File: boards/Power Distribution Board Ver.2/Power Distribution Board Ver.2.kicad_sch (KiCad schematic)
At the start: 89 parts, among them J1 Screw_Terminal_01x02, J2 Screw_Terminal_01x06, J3 Screw_Terminal_01x06, J4 Screw_Terminal_01x06, K1 Relay, K2 Relay, K3 Relay, K4 Relay, K5 Relay, K6 Relay, SW1 SW_Push_Open, U1 SIC431AED-T1-GE3, U2 SIC431AED-T1-GE3, U3 SIC431AED-T1-GE3

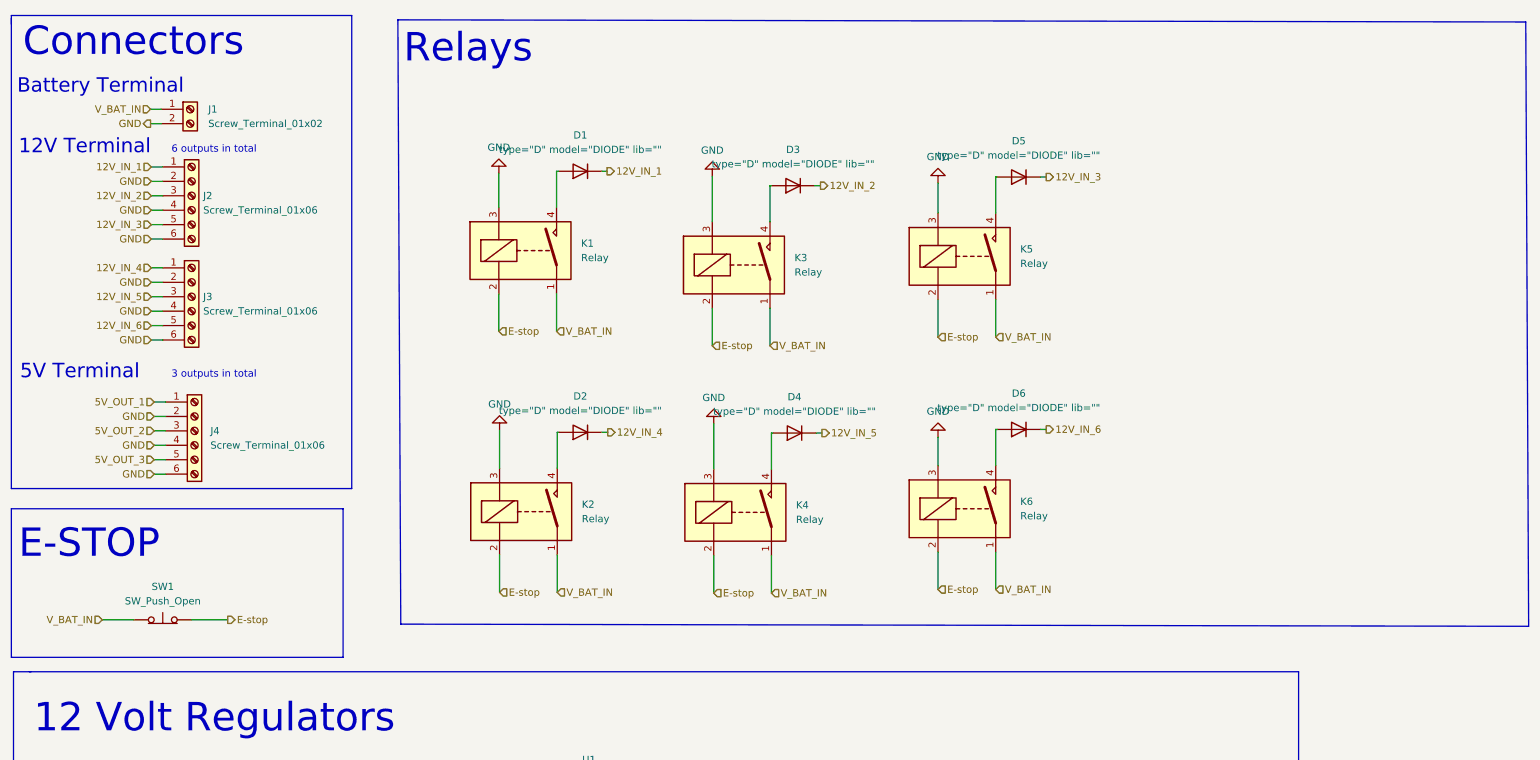
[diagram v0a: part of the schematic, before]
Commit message: 12v relay footprint and updated board wiring
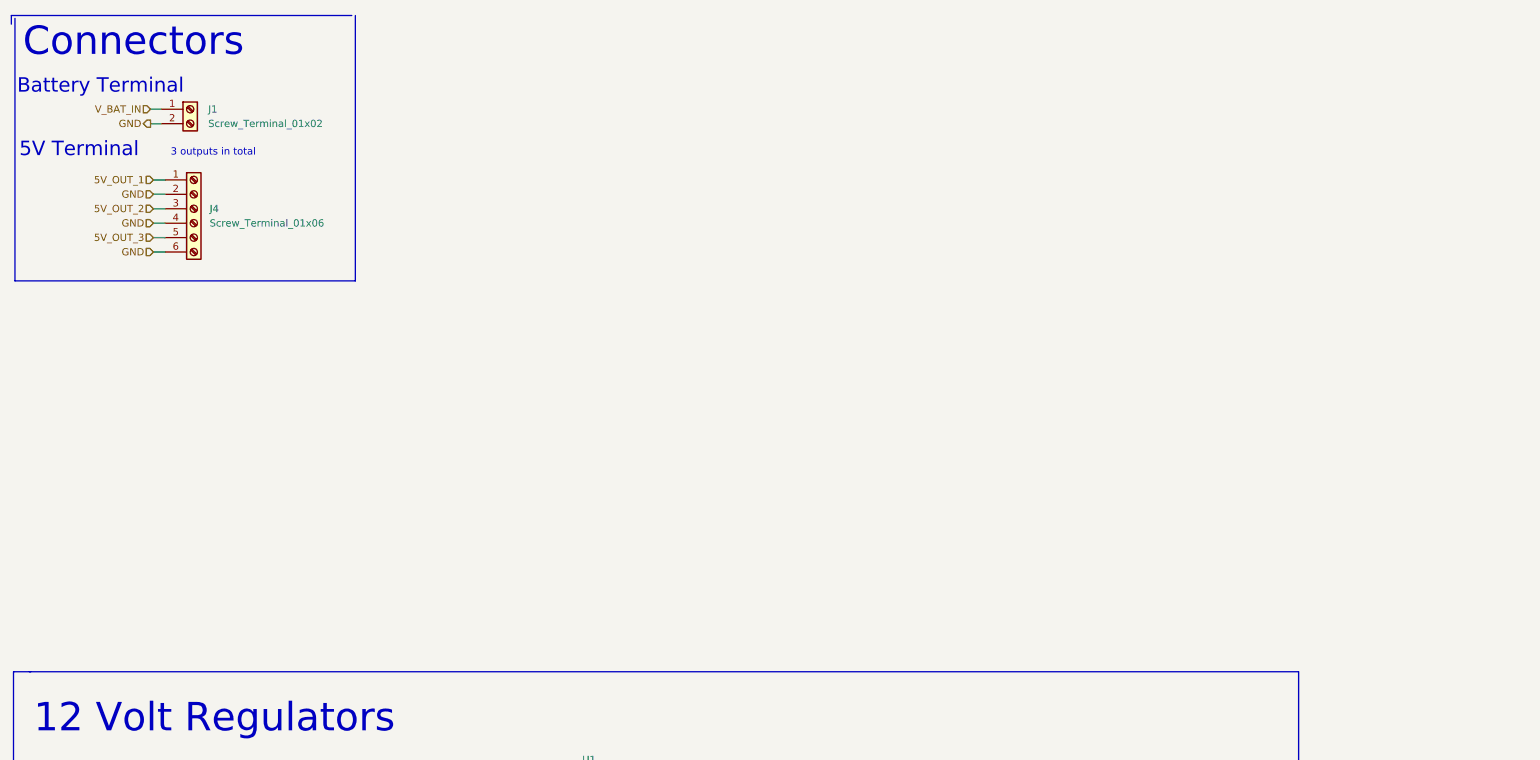
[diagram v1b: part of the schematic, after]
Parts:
- removed D1, D2, D3, D4, D5, D6: ${SIM.PARAMS}, Package_TO_SOT_SMD:TO-263-2, symbol Simulation_SPICE:DIODE
- removed J2, J3: Screw_Terminal_01x06, power_board_support:12V terminal block, symbol Connector:Screw_Terminal_01x06
- removed K1, K2, K3, K4, K5, K6: Relay, power_board_support:A10 Relay, symbol Relay:DIPxx-1Axx-11x
- removed SW1: SW_Push_Open, power_board_support:E-Stop, symbol Switch:SW_Push_Open
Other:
- note removed: "12V Terminal"
- note removed: "6 outputs in total"
- note removed: "E-STOP"
- note removed: "Relays"
- moved on the sheet: J4
